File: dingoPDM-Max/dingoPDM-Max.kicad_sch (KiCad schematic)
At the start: 6 parts

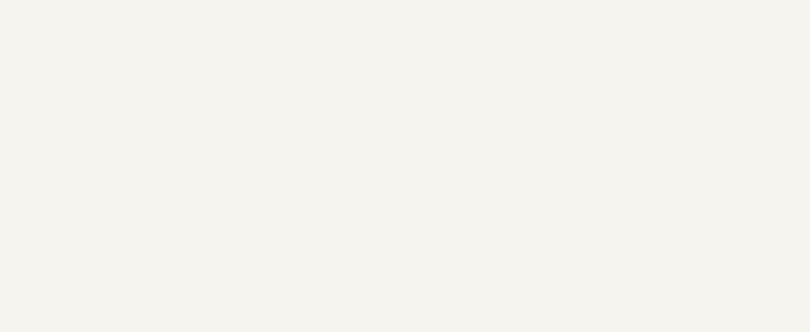
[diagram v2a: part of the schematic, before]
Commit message: add dc-dc options and 5v cap
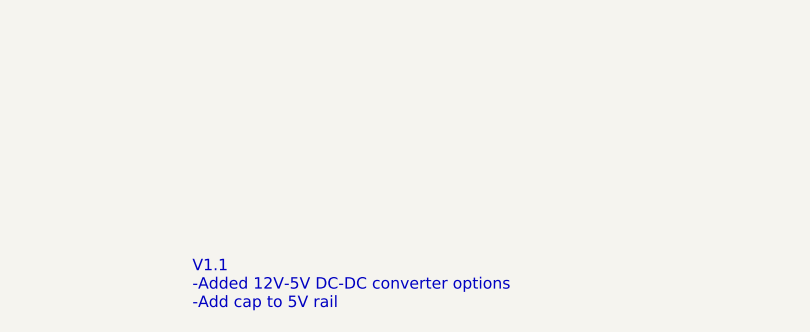
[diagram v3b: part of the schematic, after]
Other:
- note added: "V1.1 -Added 12V-5V DC-DC converter options -Add cap to 5V rail"
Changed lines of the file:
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@@
 (kicad_sch
-	(version 20231120)
+	(version 20250114)
 	(generator "eeschema")
-	(generator_version "8.0")
+	(generator_version "9.0")
 	(paper "USLetter")
 	(title_block
 		(title "dingoPDM-Max")
-		(date "2024-09-06")
-		(rev "v1.0")
+		(date "2025-06-16")
+		(rev "v1.1")
 		(comment 3 "github.com/corygrant")
 		(comment 4 "Cory Grant")
+	)
+	(text "Microcontroller"
+		(exclude_from_sim no)
+		(at 132.715 120.65 0)
+		(effects
+			(font
+				(size 1.27 1.27)
+				(thickness 0.254)
+				(bold yes)
+			)
+			(justify left bottom)
+		)
+	)
+	(text "V1.1 \n-Added 12V-5V DC-DC converter options\n-Add cap to 5V rail"
+		(exclude_from_sim no)
+		(at 87.122 191.77 0)
+		(effects
+			(font
+				(size 1.27 1.27)
+			)
+			(justify left bottom)
+		)
 	)
 	(junction
@@
 			(width 0)
 			(type default)
-		)
-	)
-	(text "Microcontroller"
-		(exclude_from_sim no)
-		(at 132.715 120.65 0)
-		(effects
-			(font
-				(size 1.27 1.27)
-				(thickness 0.254)
-				(bold yes)
-			)
-			(justify left bottom)
 		)
 	)
@@
 		(at 117.475 63.5)
 		(size 43.18 52.07)
+		(exclude_from_sim no)
+		(in_bom yes)
+		(on_board yes)
+		(dnp no)
 		(fields_autoplaced yes)
 		(stroke
@@
 		(at 231.14 19.685)
 		(size 22.86 21.59)
+		(exclude_from_sim no)
+		(in_bom yes)
+		(on_board yes)
+		(dnp no)
 		(fields_autoplaced yes)
 		(stroke
@@
 		(at 15.24 46.355)
 		(size 22.86 21.59)
+		(exclude_from_sim no)
+		(in_bom yes)
+		(on_board yes)
+		(dnp no)
 		(fields_autoplaced yes)
 		(stroke
@@
 		(at 14.605 116.84)
 		(size 22.86 21.59)
+		(exclude_from_sim no)
+		(in_bom yes)
+		(on_board yes)
+		(dnp no)
 		(fields_autoplaced yes)
 		(stroke
@@
 		(at 15.24 15.875)
 		(size 22.86 21.59)
+		(exclude_from_sim no)
+		(in_bom yes)
+		(on_board yes)
+		(dnp no)
 		(fields_autoplaced yes)
 		(stroke
@@
 		(at 14.605 144.145)
 		(size 22.86 21.59)
+		(exclude_from_sim no)
+		(in_bom yes)
+		(on_board yes)
+		(dnp no)
 		(fields_autoplaced yes)
 		(stroke
@@
 		)
 	)
+	(embedded_fonts no)
 )

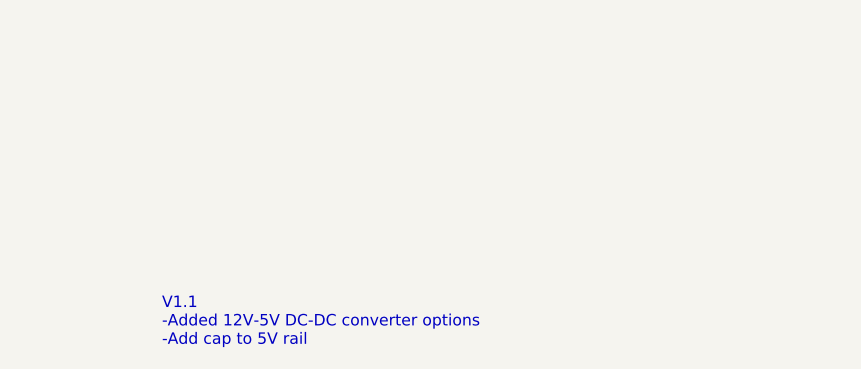
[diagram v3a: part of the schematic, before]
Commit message: fixed bad zone, shifted traces, increase trace widths
update part numbers for ibom
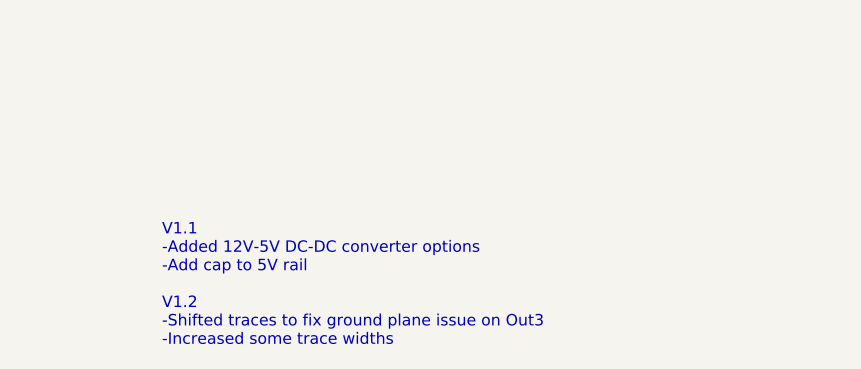
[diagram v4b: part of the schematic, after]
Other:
- note added: "V1.1 -Added 12V-5V DC-DC converter options -Add cap to 5V rail V1.2 -Shifted traces to fix ground plane issue on Out3 -Increased some trace widths"
- note removed: "V1.1 -Added 12V-5V DC-DC converter options -Add cap to 5V rail"
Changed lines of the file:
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@@
 	(title_block
 		(title "dingoPDM-Max")
-		(date "2025-06-16")
-		(rev "v1.1")
+		(date "2025-09-29")
+		(rev "v1.2")
 		(comment 3 "github.com/corygrant")
 		(comment 4 "Cory Grant")
@@
 		)
 	)
-	(text "V1.1 \n-Added 12V-5V DC-DC converter options\n-Add cap to 5V rail"
+	(text "V1.1 \n-Added 12V-5V DC-DC converter options\n-Add cap to 5V rail\n\nV1.2\n-Shifted traces to fix ground plane issue on Out3\n-Increased some trace widths"
 		(exclude_from_sim no)
 		(at 87.122 191.77 0)
